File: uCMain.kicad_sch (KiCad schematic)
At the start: 1 part, among them U1 STM32H745ZGT6

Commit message: v2.0 schematics updated
1. Need to be tested for errors
2. PCB layout is not started yet
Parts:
- added C401, C409, C411, C412, C413, C414, C415, C416, C417, C418, C419, C420, C421, C422, C423, C424, C427, C429, C432: 100n, Capacitor_SMD:C_0402_1005Metric, symbol Device:C
- added C402, C404, C428: 10u, Capacitor_SMD:C_0402_1005Metric, symbol Device:C
- added C403: 220p, Capacitor_SMD:C_0402_1005Metric, symbol Device:C
- added C405, C406, C425: 4u7, Capacitor_SMD:C_0402_1005Metric, symbol Device:C
- added C407, C408: 2u2, Capacitor_SMD:C_0402_1005Metric, symbol Device:C
- added C410, C426: 1u, Capacitor_SMD:C_0402_1005Metric, symbol Device:C
- added C430, C434: 5.6pF, symbol Device:C
- added C431, C433: 5p6, Capacitor_SMD:C_0402_1005Metric, symbol Device:C
- added D401, D402, D403, D404, D405: PESD3V3L1BA,115, EMS:PESD3V3L1BA_115-SOD-323-2, symbol EMS:PESD3V3L1BA,115
- added D406: LED_RAGB, LED_SMD:LED_Kingbright_APFA3010_3x1.5mm_Horizontal, symbol Device:LED_RAGB
- added D407, D408: ESDALC6V1-1M2, EMS:ESDALC6V11M2, symbol EMS:ESDALC6V1-1M2
- added FB401: FerriteBead, Inductor_SMD:L_0603_1608Metric, symbol Device:FerriteBead
- added J401: Conn_02x05_Counter_Clockwise, EMS:62701021621, symbol Connector_Generic:Conn_02x05_Odd_Even
- added JP401, JP402, JP403, JP406: SolderJumper_2_Bridged, symbol Jumper:SolderJumper_2_Bridged
- added JP404, JP405, JP407: SolderJumper_2_Open, symbol Jumper:SolderJumper_2_Open
- added L401: L, symbol Device:L
- added L402: 2u2, symbol Device:L
- added R401, R406, R407: 22R, Resistor_SMD:R_0603_1608Metric, symbol Device:R
- added R402, R403, R404, R405: 49R9, Resistor_SMD:R_0402_1005Metric, symbol Device:R
- added R408, R409, R410: 1k, Resistor_SMD:R_0603_1608Metric, symbol Device:R
- added R411: 10k, Resistor_SMD:R_0603_1608Metric, symbol Device:R
- added SW401, SW402: SW_Push, Button_Switch_SMD:SW_SPST_CK_RS282G05A3, symbol Switch:SW_Push
- added unit 2 of U401
- added Y401: 32.768KHz, Crystal:Crystal_SMD_3215-2Pin_3.2x1.5mm, symbol Device:Crystal
- added Y402: Crystal_GND24, EMS:NX3225SA25000MSTDCSR6, symbol Device:Crystal_GND24
- renumbered U1 to U401
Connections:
- net ADS_SPI_SCK: now reaches U401.1 (PE2)
- net OSC32_IN: now reaches U401.10 (PC14-OSC32_IN)
- net OSC32_IN: now also C431.1, Y401.1
- net uC_OTG_D-: now reaches U401.100 (PA11)
- net uC_OTG_D+: now reaches U401.101 (PA12)
- net DEBUG_JTMS-SWDIO: now reaches U401.102 (PA13)
- net DEBUG_JTMS-SWDIO: now also R402.1
- net DEBUG_JTCK-SWCLK: now reaches U401.107 (PA14)
- net DEBUG_JTCK-SWCLK: now also R403.1
- net UART4_DE: now reaches U401.108 (PA15)
- net SDMMC1_D2: now reaches U401.109 (PC10)
- net OSC32_OUT: now reaches U401.11 (PC15-OSC32_OUT)
- net OSC32_OUT: now also C433.1, Y401.2
- net SDMMC1_D3: now reaches U401.110 (PC11)
- net SDMMC1_CK: now reaches U401.111 (PC12)
- net UART4_RX: now reaches U401.112 (PD0)
- net USART2_INV_485: now reaches U401.113 (PD1)
- net SDMMC1_CMD: now reaches U401.114 (PD2)
- net USART2_DE: now reaches U401.116 (PD4)
- net USART2_TX: now reaches U401.117 (PD5)
- net SDMMC2_CK: now reaches U401.120 (PD6)
- net SDMMC2_CMD: now reaches U401.121 (PD7)
- net at U401.122 (PG9): now also R401.2
- net SD_DETECT: now reaches U401.123 (PG10)
- net SDMMC2_D2: now reaches U401.124 (PG11)
- net RMII_TXD1: now reaches U401.125 (PG12)
- net RMII_TXD0: now reaches U401.126 (PG13)
- net DEBUG_JTDO-SWO: now reaches U401.130 (PB3)
- net DEBUG_JTDO-SWO: now also R404.1
- net SDMMC2_D3: now reaches U401.131 (PB4)
- net SPI1_MOSI: now reaches U401.132 (PB5)
- net I2C1_SCL: now reaches U401.133 (PB6)
- net I2C1_SDA: now reaches U401.134 (PB7)
- net BOOT0: now reaches U401.135 (BOOT0)
- net BOOT0: now also D407.1 (K), R411.2, SW402.1
- net SDMMC1_D4: now reaches U401.136 (PB8)
- net SDMMC1_D5: now reaches U401.137 (PB9)
- net eMMC_RSTn: now reaches U401.138 (PE0)
- net BLE_INT: now reaches U401.2 (PE3)
- net ADS_CS: now reaches U401.20 (PF6)
- net at U401.21 (PF7): now also R406.1
- net SPI5_MISO: now reaches U401.22 (PF8)
- net at U401.23 (PF9): now also R407.1
- net SPI5_CS: now reaches U401.24 (PF10)
- net OSC_IN: now reaches U401.25 (PH0-OSC_IN)
- net OSC_IN: now also C434.2, Y402.1
- net OSC_OUT: now reaches U401.26 (PH1-OSC_OUT)
- net OSC_OUT: now also C430.2, Y402.3
- net NRST: now reaches U401.27 (NRST)
- net NRST: now also C401.1, C432.1, D408.1 (K), R405.1, SW401.1
- net ADS_SYNC_RESET: now reaches U401.28 (PC0)
- net RMII_MDC: now reaches U401.29 (PC1)
- net ADC3_INP1: now reaches U401.31 (PC3_C)
- net UART4_TX: now reaches U401.37 (PA0)
- net RMII_REF_CLK: now reaches U401.38 (PA1)
- net RMII_MDIO: now reaches U401.39 (PA2)
- net ADS_DOUT_uC_DIN: now reaches U401.4 (PE5)
- net USART2_RX: now reaches U401.40 (PA3)
- net SPI1_NSS: now reaches U401.43 (PA4)
- net SPI1_SCK: now reaches U401.44 (PA5)
- net ETH_NRST: now reaches U401.45 (PA6)
- net RMII_CRS_DV: now reaches U401.46 (PA7)
- net RMII_RXD0: now reaches U401.47 (PC4)
- net RMII_RXD1: now reaches U401.48 (PC5)
- net ADC1_INP9: now reaches U401.49 (PB0)
- net ADS_DIN_uC_DOUT: now reaches U401.5 (PE6)
- net LDO_EN: now reaches U401.52 (PF11)
- net DCDC_2_EN: now reaches U401.53 (PF14)
- net TIM1_CH1: now reaches U401.59 (PE9)
- net TIM1_CH1: now also R408.2
- net GPIO_OUT_1: now reaches U401.60 (PE10)
- net TIM1_CH2: now reaches U401.61 (PE11)
- net TIM1_CH2: now also R409.2
- net GPIO_IN_1: now reaches U401.62 (PE12)
- net TIM1_CH3: now reaches U401.63 (PE13)
- net TIM1_CH3: now also R410.2
- net GPIO_IN_2: now reaches U401.64 (PE14)
- net RMII_TX_EN: now reaches U401.67 (PB12)
- net FDCAN2_TX: now reaches U401.73 (PB13)
- net SDMMC2_D0: now reaches U401.74 (PB14)
- net SDMMC2_D1: now reaches U401.75 (PB15)
- net BLE_RST: now reaches U401.76 (PD8)
- net BLE_TEST9: now reaches U401.77 (PD9)
- net BLE_TEST8: now reaches U401.78 (PD10)
- net TIM4_CH1: now reaches U401.82 (PD12)
- net TIM4_CH2: now reaches U401.83 (PD13)
- net ADS_DRDY: now reaches U401.9 (PC13)
- net SDMMC1_D6: now reaches U401.93 (PC6)
- net SDMMC1_D7: now reaches U401.94 (PC7)
- net SDMMC1_D0: now reaches U401.95 (PC8)
- net SDMMC1_D1: now reaches U401.96 (PC9)
- net ADS_STM32_CLKOUT: now reaches U401.97 (PA8)
- new net: C403.2, L402.2, U401.15 (VLXSMPS)
- new net: D406.1 (RK), R408.1
- new net: D406.3 (GK), R409.1
- new net: D406.4 (BK), R410.1
- new net: D405.2 (K2), J401.10 (Pin_10), R405.2
- new net: D404.2 (K2), J401.6 (Pin_6), R404.2
- new net: C402.2, L401.2, U401.16 (VDDSMPS)
- new net: D402.2 (K2), J401.2 (Pin_2), R402.2
- new net: D403.2 (K2), J401.4 (Pin_4), R403.2
- new net: JP402.2 (B), JP403.2 (B), JP404.2 (B), JP405.2 (B), U401.103 (VCAP_2), U401.140 (VCAP_3), U401.68 (VCAP_1)
- new net: JP406.2 (B), JP407.2 (B), U401.105 (VDDLDO_2), U401.143 (VDDLDO_3), U401.70 (VDDLDO_1)
- new net: C404.2, JP401.1 (A)
- new net: C407.2, JP404.1 (A)
- new net: C408.2, JP405.1 (A)
- new net +DCDC_1: C409.1, C410.1, C411.1, C412.1, C413.1, C414.1, C415.1, C416.1, C417.1, C418.1, C419.1, C420.1, C421.1, C422.1, C423.1, C424.1, C425.1, D401.2 (K2), D406.2 (A), FB401.1, J401.1 (Pin_1), JP407.1 (A), L401.1, SW402.2, U401.106 (VDD_10), U401.119 (VDD_11), U401.129 (VDD_12), U401.13 (VDD_2), U401.144 (VDD_13), U401.19 (VDD_3), U401.32 (VDD_4), U401.42 (VDD_5), U401.56 (VDD_6), U401.7 (VDD_1), U401.71 (VDD_7), U401.79 (VDD_8), U401.90 (VDD50USB), U401.91 (VDD33USB), U401.92 (VDD_9)
- new net +VDD_SDC: C405.2, C406.2, JP401.2 (B), JP402.1 (A), JP403.1 (A), JP406.1 (A), L402.1, U401.17 (VFBSMPS)
- new net +VREF: C426.1, C427.1, C428.1, C429.1, FB401.2, U401.35 (VREF+), U401.36 (VDDA)
- new net FDCAN2_RX: U401.67 (PB12)
- new net GND: C401.2, C402.1, C403.1, C404.1, C405.1, C406.1, C407.1, C408.1, C409.2, C410.2, C411.2, C412.2, C413.2, C414.2, C415.2, C416.2, C417.2, C418.2, C419.2, C420.2, C421.2, C422.2, C423.2, C424.2, C425.2, C426.2, C427.2, C428.2, C429.2, C430.1, C431.2, C432.2, C433.2, C434.1, D401.1 (K1), D402.1 (K1), D403.1 (K1), D404.1 (K1), D405.1 (K1), D407.2 (A), D408.2 (A), J401.3 (Pin_3), J401.5 (Pin_5), J401.9 (Pin_9), R411.1, SW401.2, U401.104 (VSS_10), U401.118 (VSS_11), U401.12 (VSS_2), U401.128 (VSS_12), U401.14 (VSSSMPS), U401.141 (VSS_13), U401.18 (VSS_3), U401.33 (VSS_4), U401.34 (VSSA), U401.41 (VSS_5), U401.55 (VSS_6), U401.6 (VSS_1), U401.69 (VSS_7), U401.80 (VSS_8), U401.89 (VSS_9), Y402.2, Y402.4
- new net SPI1_MISO: R401.1
- new net SPI5_MOSI: R407.2
- new net SPI5_SCK: R406.2
- no-connect marks 0 -> 2
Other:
- note added: "BOOT0"
- note added: "Crystal Oscillator"
- note added: "MCU-Pinout"
- note added: "MCU-Power"
- note added: "Power Supply Bypass Capacitors"
- note added: "RESET"
- note added: "RGB LED"
- note added: "SWD Header"
- note added: "Switch - RESET & BOOT0"
- company: (none) -> Manufacturing Innovation Network Laboratory (MINLab)
- title: (none) -> Energy Monitoring System

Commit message: minor formatting updates
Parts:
- renumbered C432 to C401, C412 to C402, C413 to C403, C414 to C404, C404 to C405, C410 to C406, C415 to C407, C430 to C408, C434 to C409, C405 to C410, C406 to C411, C407 to C412, C408 to C413, C411 to C414, C402 to C415, C403 to C419, C419 to C420, C420 to C421, C421 to C422, C431 to C423, C433 to C424, C422 to C425, C423 to C426, C424 to C427, C425 to C428, C426 to C429, C427 to C430, C428 to C431, C429 to C432, C409 to C433, C401 to C434, D408 to D401, D407 to D402, D401 to D403, D402 to D404, D403 to D405, D404 to D406, D406 to D407, D405 to D408, R406 to R401, R407 to R402, R401 to R403, R411 to R404, R408 to R405, R409 to R406, R410 to R407, R402 to R408, R403 to R409, R404 to R410, R405 to R411, Y402 to Y401, Y401 to Y402

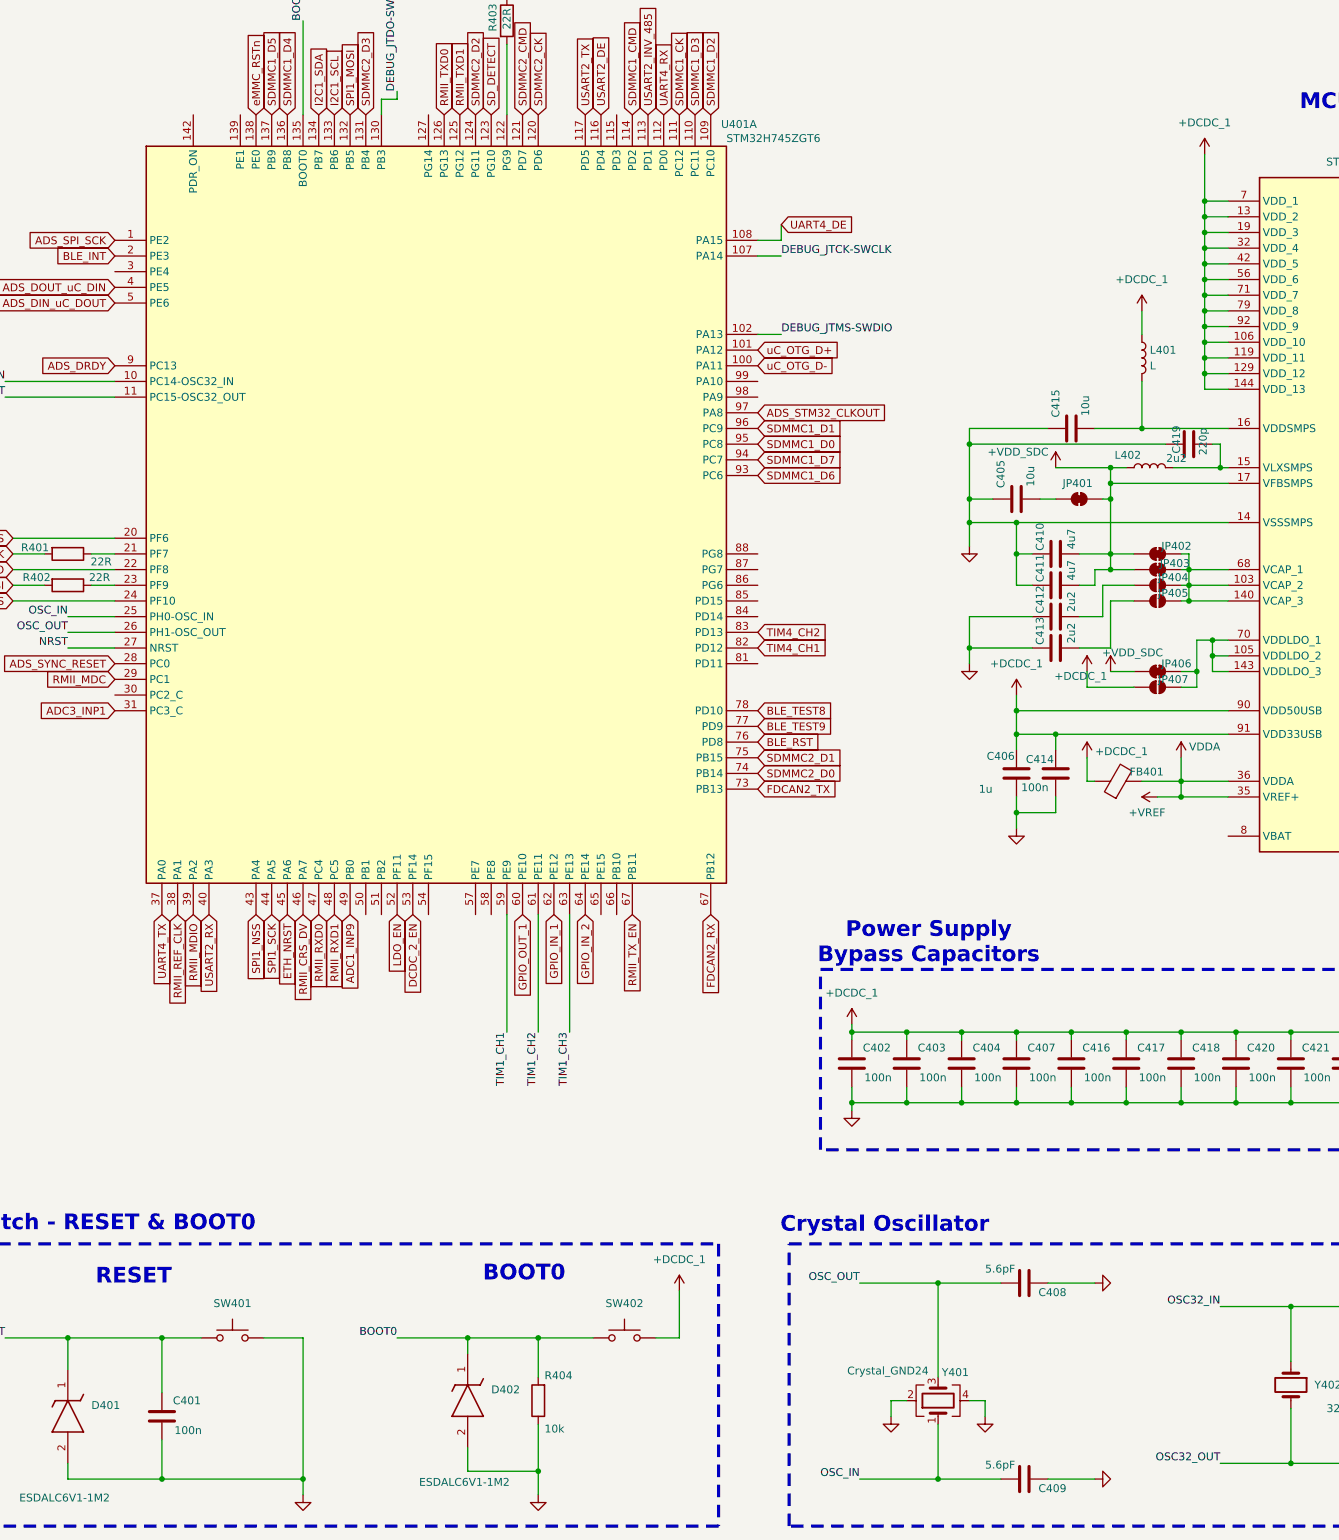
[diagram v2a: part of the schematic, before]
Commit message: schematics errors fixed and ready for PCB
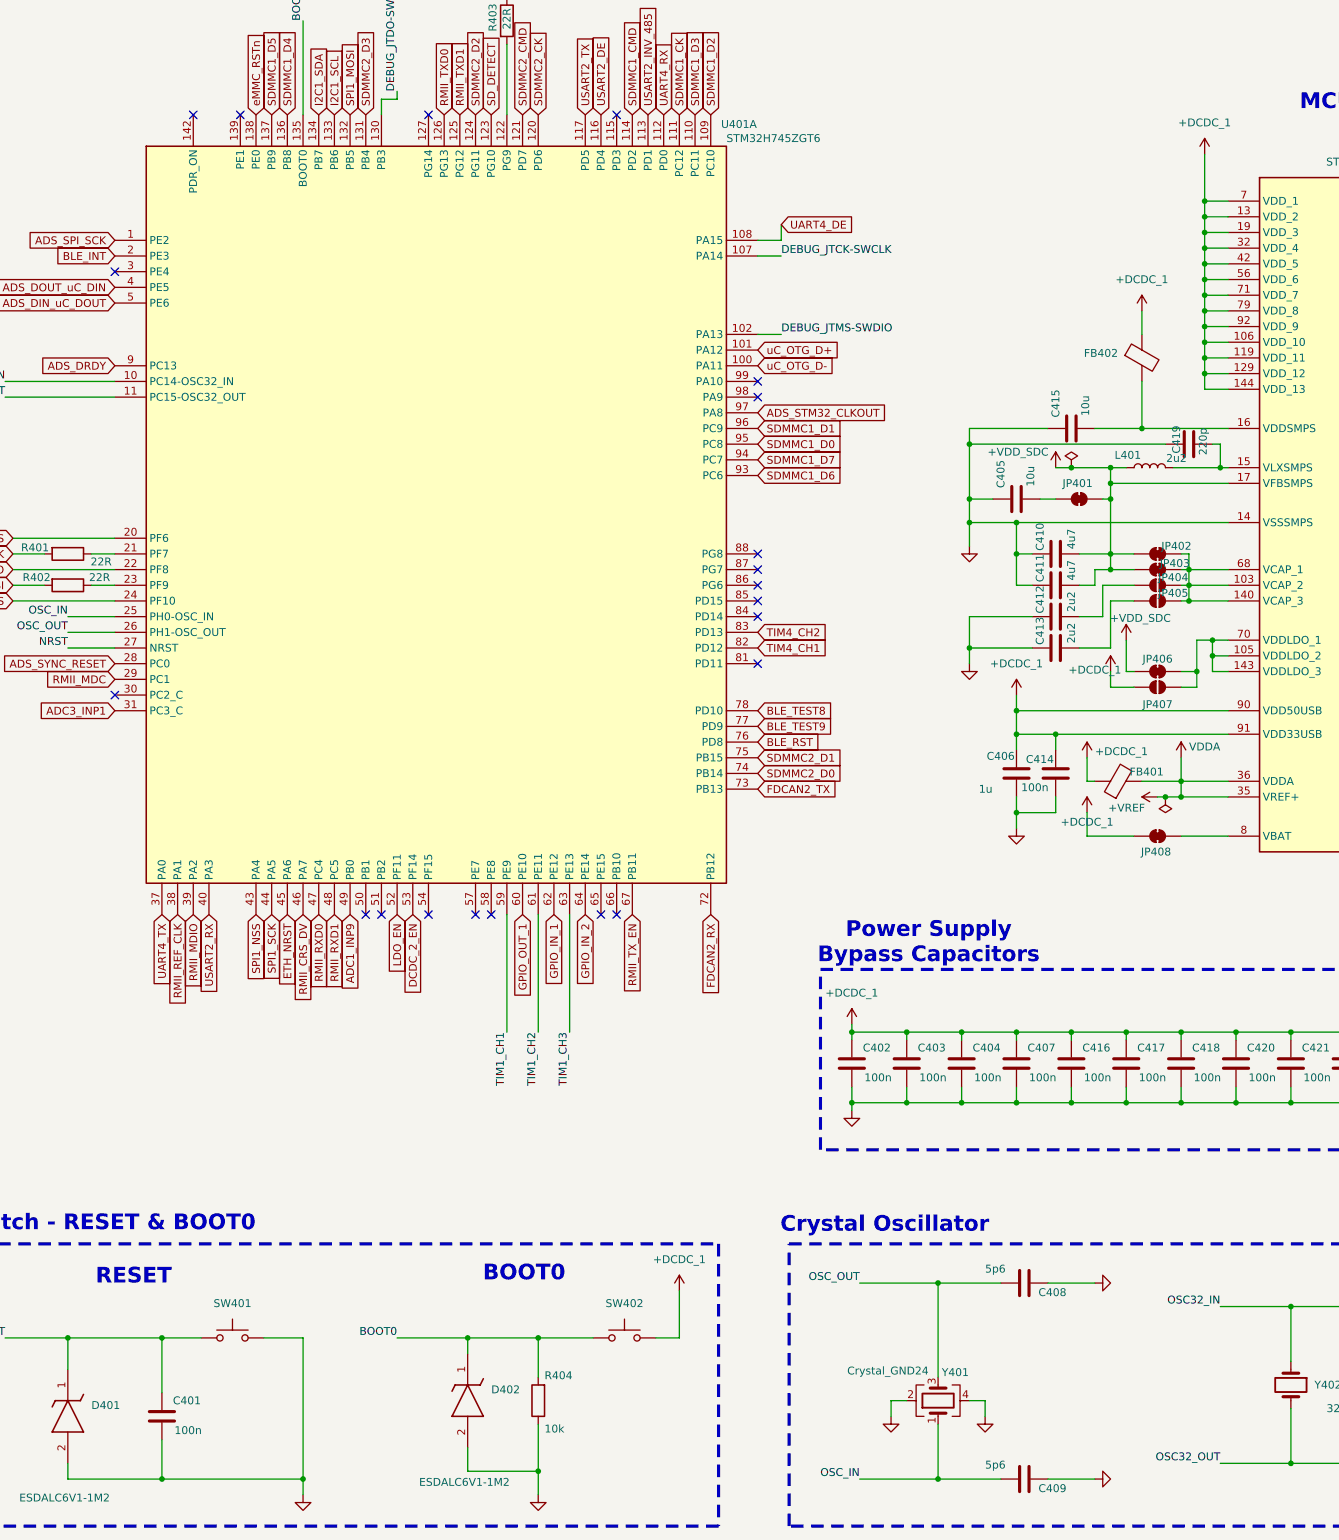
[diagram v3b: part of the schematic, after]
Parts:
- removed L401: L, symbol Device:L
- added FB402: FerriteBead, Inductor_SMD:L_0603_1608Metric, symbol Device:FerriteBead
- added JP408: SolderJumper_2_Bridged, Jumper:SolderJumper-2_P1.3mm_Bridged_RoundedPad1.0x1.5mm, symbol Jumper:SolderJumper_2_Bridged
- C405, C415, C431: footprint Capacitor_SMD:C_0402_1005Metric -> Capacitor_SMD:C_0603_1608Metric; Distributor_Link https://www.mouser.com/ProductDetail/KYOCERA-AVX/04023C104K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 -> https://www.mouser.com/ProductDetail/KYOCERA-AVX/KGM15CR51A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; Manufacturer_Part_Number 04023C104KAT2A -> KGM15CR51A106KT
- C406, C429: Distributor_Link https://www.mouser.com/ProductDetail/KYOCERA-AVX/04023C104K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 -> https://www.mouser.com/ProductDetail/KYOCERA-AVX/KGM05AR70J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; Manufacturer_Part_Number 04023C104KAT2A -> KGM05AR70J105KH
- C408, C409: value 5.6pF -> 5p6; footprint (none) -> Capacitor_SMD:C_0402_1005Metric; Distributor_Link (none) -> https://www.mouser.com/ProductDetail/Murata-Electronics/GJM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; Manufacturer_Name (none) -> Murata Electronics; Manufacturer_Part_Number (none) -> GJM1555C1H5R6FB01D
- C412, C413: Distributor_Link https://www.mouser.com/ProductDetail/KYOCERA-AVX/04023C104K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 -> https://www.mouser.com/ProductDetail/KYOCERA-AVX/KGM05AR51A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
- C419: Distributor_Link https://www.mouser.com/ProductDetail/KYOCERA-AVX/04023C104K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 -> https://www.mouser.com/ProductDetail/YAGEO/CC0402JRNPO9BN22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; Manufacturer_Name KYOCERA AVX -> YAGEO; Manufacturer_Part_Number 04023C104KAT2A -> CC0402JRNPO9BN221
- JP401, JP402, JP403, JP406: footprint (none) -> Jumper:SolderJumper-2_P1.3mm_Bridged_RoundedPad1.0x1.5mm
- JP404, JP405, JP407: footprint (none) -> Jumper:SolderJumper-2_P1.3mm_Open_RoundedPad1.0x1.5mm
- L401: renamed from L402; footprint (none) -> Inductor_SMD:L_0603_1608Metric; Distributor_Link (none) -> https://www.mouser.com/ProductDetail/TAIYO-YUDEN/MCHK1608T2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; Manufacturer_Name (none) -> TAIYO YUDEN; Manufacturer_Part_Number (none) -> MCHK1608T2R2MKN
- U401: Distributor_Link (none) -> https://www.arrow.com/en/products/stm32h745zgt6/stmicroelec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
- Y401: Distributor_Link (none) -> https://www.mouser.com/ProductDetail/NDK/NX3225SA-25.000M-S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; Manufacturer_Name (none) -> NDK; Manufacturer_Part_Number (none) -> NX3225SA-25.000M-STD-CSR-6
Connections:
- net +DCDC_1: now also FB402.1, JP408.1 (A)
- net FDCAN2_RX: now also U401.72 (PB12); no longer U401.67 (PB12)
- net at C415.2, U401.16 (VDDSMPS): now also FB402.2
- net at U401.8 (VBAT): now also JP408.2 (B)
- no-connect marks 2 -> 23

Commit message: new version created. Now at v2.0.0
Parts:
- added C435: 2u2, Capacitor_SMD:C_0402_1005Metric, symbol Device:C
- C428: value 4u7 -> 2u2; Distributor_Link https://www.mouser.com/ProductDetail/KYOCERA-AVX/04023C104K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 -> https://www.mouser.com/ProductDetail/KYOCERA-AVX/KGM05AR51A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
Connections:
- net +DCDC_1: now also C428.2, C435.2; no longer C428.1
- net GND: now also C428.1, C435.1; no longer C428.2
- net NRST-H: now reaches D408.2 (K2), J401.10 (Pin_10), R411.2
- net DEBUG_JTDO-SWO-H: now reaches D406.2 (K2), J401.6 (Pin_6), R410.2
- net DEBUG_JTMS-SWDIO-H: now reaches D404.2 (K2), J401.2 (Pin_2), R408.2
- net DEBUG_JTCK-SWCLK-H: now reaches D405.2 (K2), J401.4 (Pin_4), R409.2
- net SPI5_SCK_R: now reaches R401.1, U401.21 (PF7)
- net SPI5_MOSI_R: now reaches R402.1, U401.23 (PF9)

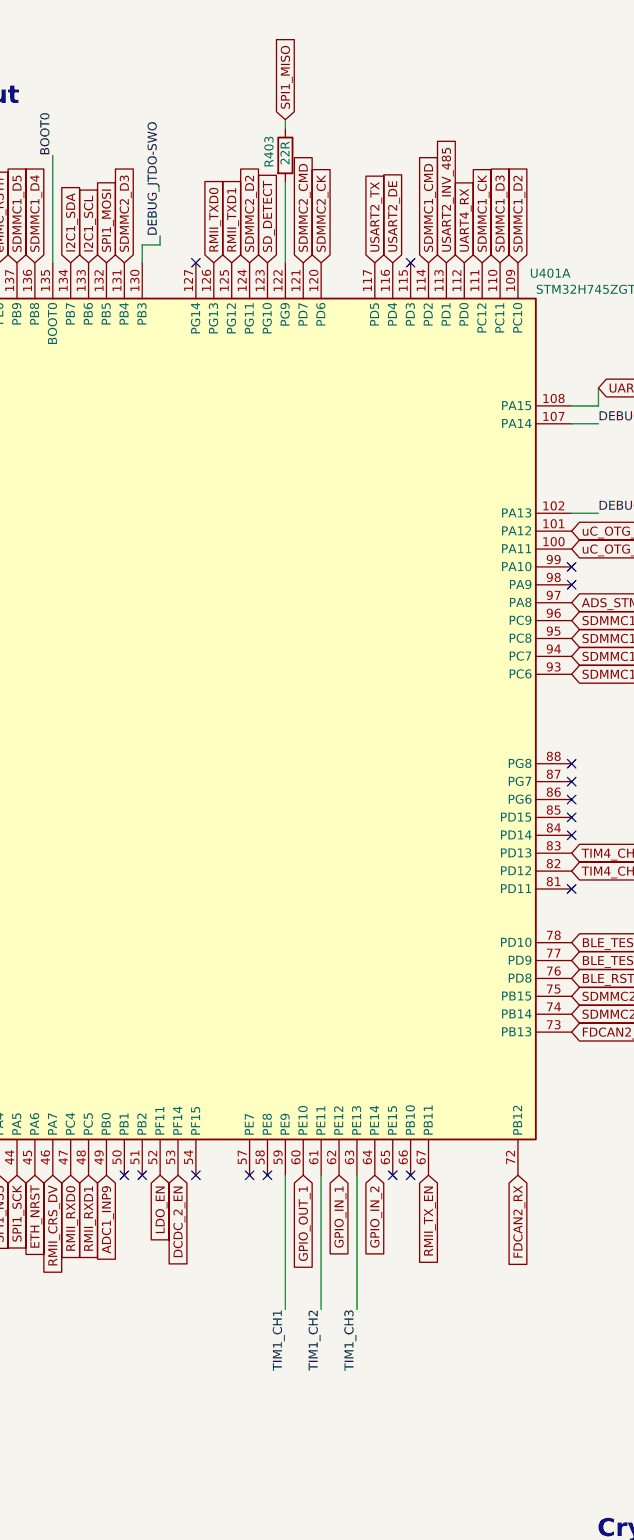
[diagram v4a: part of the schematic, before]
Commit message: validation BOM
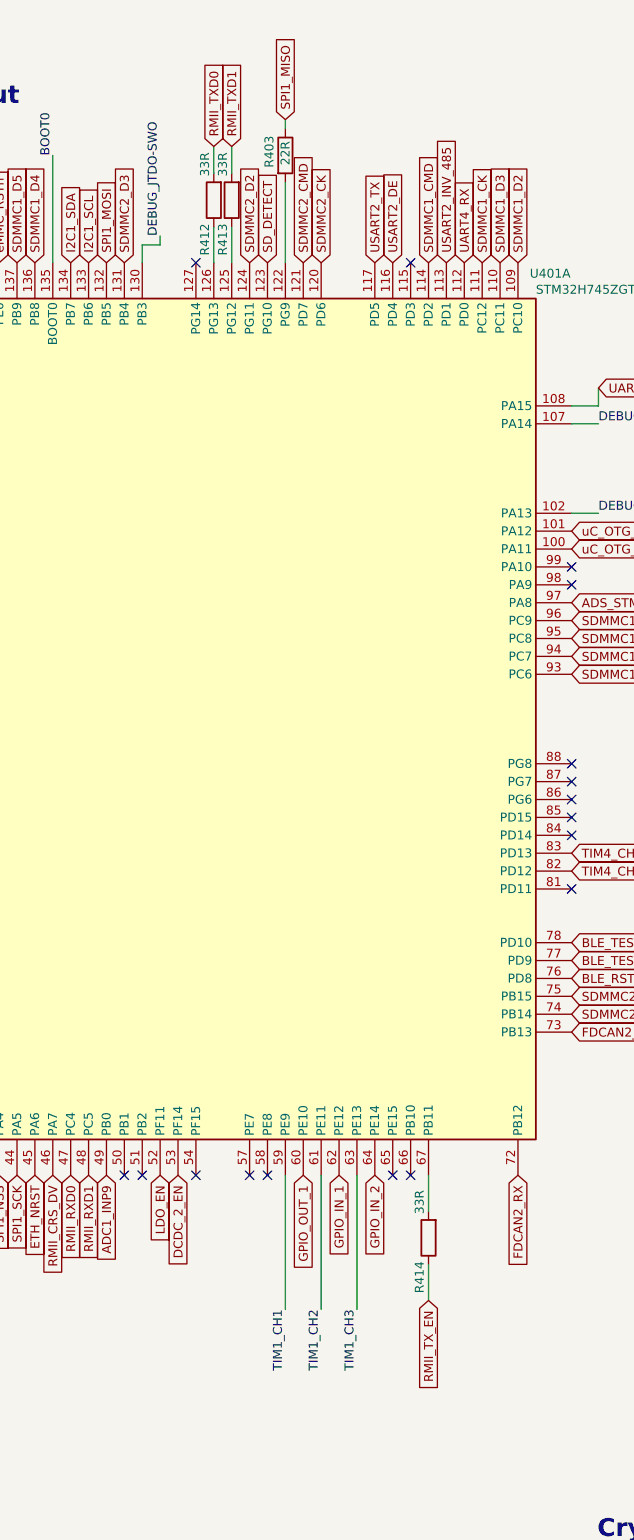
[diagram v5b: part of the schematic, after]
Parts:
- added R412, R413, R414: 33R, Resistor_SMD:R_0603_1608Metric, symbol Device:R
- C406, C429: Manufacturer_Name KYOCERA AVX -> KYOCERA AVX
- C410, C411: Distributor_Link https://www.mouser.com/ProductDetail/KYOCERA-AVX/04023C104K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 -> https://www.mouser.com/ProductDetail/KYOCERA-AVX/KAM05CT70J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; Manufacturer_Part_Number 04023C104KAT2A -> KAM05CT70J475KH
- SW401, SW402: Distributor_Link https://www.mouser.com/ProductDetail/CK/RS282G05A3SMRT?qs=G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 -> https://www.mouser.com/ProductDetail/CK/RS-282G05A3-SM-RT?q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
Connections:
- net RMII_TXD0: now also R412.2; no longer U401.126 (PG13)
- net RMII_TXD1: now also R413.2; no longer U401.125 (PG12)
- net RMII_TX_EN: now also R414.1; no longer U401.67 (PB11)
- new net: R414.2, U401.67 (PB11)
- new net: R412.1, U401.126 (PG13)
- new net: R413.1, U401.125 (PG12)
